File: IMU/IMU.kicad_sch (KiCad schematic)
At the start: 4 parts, among them IC1 ADXL326BCPZ-RL7, U1 DEV-16771, U2 IAM-20380, U3 MLX90393SLW-ABA-011-RE

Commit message: Finished Schematic!!!
Co-Authored-By: Ram Godbole <91348559+EnderScythe@users.noreply.github.com>
Co-Authored-By: Ayaan-Abrol <89829573+Ayaan-Abrol@users.noreply.github.com>
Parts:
- added C1, C2, C3: 3 nF, Capacitor_SMD:C_0603_1608Metric, symbol Device:C
- added C10, C6, C9: 0.1 uF, Capacitor_SMD:C_0603_1608Metric, symbol Device:C
- added C4: 0.01 uF, Capacitor_SMD:C_0603_1608Metric, symbol Device:C
- added C5: 0.47 uF, Capacitor_SMD:C_0603_1608Metric, symbol Device:C
- added C7: 2.2 uF, Capacitor_SMD:C_0603_1608Metric, symbol Device:C
- added C8: 10 nF, Capacitor_SMD:C_0603_1608Metric, symbol Device:C
- IC1: footprint ADXL326BCPZRL7 -> ADXL326BCPZ-RL7:ADXL326BCPZRL7
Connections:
- net 3P3V: now reaches U2.1 (VDDIO)
- net 3P3V: now also IC1.14 (VS_1), IC1.15 (VS_2), U1.3.3V_1 (3.3V), U1.3.3V_2 (3.3V__1), U1.3.3V_3 (3.3V__2), U2.16 (VDD), U3.15 (VDD), U3.8 (VDD_IO), C10.1, C4.1, C6.1, C7.1, C8.1, C9.1
- net GND: now reaches U2.10 (RESV)
- net GND: now also IC1.17 (EP), IC1.3 (COM_1), IC1.5 (COM_2), IC1.6 (COM_3), IC1.7 (COM_4), U2.11 (RESV), U2.12 (RESV), U2.13 (GND), U2.15 (RESV), U2.8 (FSYNC), U2.9 (RESV), U3.11 (A1), U3.12 (A0), U3.13 (VSS), U3.17 (GND), C1.2, C10.2, C2.2, C3.2, C4.2, C5.2, C6.2, C7.2, C8.2, C9.2
- net at U2.14 (REGOUT): now also C5.1
- net SCK_Gyro: now reaches U2.2 (SCL/SPC)
- net SCK_Gyro: now also U1.27 (A13)
- net MOSI_Gyro: now reaches U2.3 (SDA/SDI)
- net MOSI_Gyro: now also U1.26 (A12)
- net MISO_Gyro: now reaches U2.4 (SA0/SDO)
- net MISO_Gyro: now also U1.1 (TX1)
- net CS_Gyro: now reaches U2.5 (CS)
- net CS_Gyro: now also U1.0 (RX1)
- net INT_Gyro: now reaches U2.6 (INT)
- net INT_Gyro: now also U1.17 (A3)
- net CS_Mag: now reaches U1.10 (CS1)
- net CS_Mag: now also U3.2 (SENB/CS)
- net MOSI_Mag: now reaches U1.11 (MOSI)
- net MOSI_Mag: now also U3.5 (SDA/MOSI)
- net MISO_Mag: now reaches U1.12 (MISO)
- net MISO_Mag: now also U3.6 (MISO)
- net SCK_Mag: now reaches U1.13 (SCK)
- net SCK_Mag: now also U3.3 (SCL/SCLK)
- net X_Accel: now reaches U1.14 (A0)
- net X_Accel: now also IC1.12 (XOUT), C1.1
- net Y_Accel: now reaches U1.15 (A1)
- net Y_Accel: now also IC1.10 (YOUT), C2.1
- net Z_Accel: now reaches U1.16 (A2)
- net Z_Accel: now also IC1.8 (ZOUT), C3.1
- net INT_Mag: now reaches U1.18 (A4)
- net INT_Mag: now also U3.1 (INT)
- net TRIG_Mag: now reaches U1.19 (A5)
- net TRIG_Mag: now also U3.7 (INT/TRIG)
- no-connect marks 0 -> 7
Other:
- note added: "Accelerometer"
- note added: "Gyroscope"
- note added: "Magnetometer"
- moved on the sheet: U2

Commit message: Ground is important!
Co-Authored-By: Ram Godbole <91348559+EnderScythe@users.noreply.github.com>
Co-Authored-By: Ayaan-Abrol <89829573+Ayaan-Abrol@users.noreply.github.com>
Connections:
- net GND: now also U1.GND1 (GND), U1.GND2 (GND__1), U1.GND3 (GND__2), U1.GND4 (GND__3), U1.GND5 (GND__4), U1.USB_GND1 (USB_GND), U1.USB_GND2 (USB_GND__1)
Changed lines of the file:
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@@
+	)
+	(junction
+		(at 63.5 139.7)
+		(diameter 0)
+		(color 0 0 0 0)
 	)
 	(junction
@@
 	)
 	(junction
+		(at 63.5 134.62)
+		(diameter 0)
+		(color 0 0 0 0)
+	)
+	(junction
+		(at 63.5 142.24)
+		(diameter 0)
+		(color 0 0 0 0)
+	)
+	(junction
 		(at 219.71 90.17)
 		(diameter 0)
@@
 	)
 	(junction
+		(at 63.5 129.54)
+		(diameter 0)
+		(color 0 0 0 0)
+	)
+	(junction
 		(at 168.91 63.5)
 		(diameter 0)
@@
 	)
 	(junction
+		(at 63.5 137.16)
+		(diameter 0)
+		(color 0 0 0 0)
+	)
+	(junction
 		(at 224.79 45.72)
 		(diameter 0)
@@
 	(junction
 		(at 63.5 30.48)
+		(diameter 0)
+		(color 0 0 0 0)
+	)
+	(junction
+		(at 63.5 132.08)
 		(diameter 0)
 		(color 0 0 0 0)
@@
 	(wire
 		(pts
+			(xy 63.5 142.24) (xy 63.5 147.32)
+		)
+		(stroke
+			(width 0)
+			(type default)
+		)
+	)
+	(wire
+		(pts
 			(xy 248.92 73.66) (xy 245.11 73.66)
 		)
@@
 	(wire
 		(pts
+			(xy 63.5 137.16) (xy 63.5 139.7)
+		)
+		(stroke
+			(width 0)
+			(type default)
+		)
+	)
+	(wire
+		(pts
 			(xy 226.06 105.41) (xy 226.06 110.49)
 		)
@@
 	(wire
 		(pts
+			(xy 63.5 127) (xy 63.5 129.54)
+		)
+		(stroke
+			(width 0)
+			(type default)
+		)
+	)
+	(wire
+		(pts
 			(xy 168.91 63.5) (xy 168.91 66.04)
 		)
@@
 	(wire
 		(pts
+			(xy 63.5 132.08) (xy 63.5 134.62)
+		)
+		(stroke
+			(width 0)
+			(type default)
+		)
+	)
+	(wire
+		(pts
 			(xy 242.57 90.17) (xy 250.19 90.17)
 		)
@@
 	(wire
 		(pts
+			(xy 63.5 129.54) (xy 63.5 132.08)
+		)
+		(stroke
+			(width 0)
+			(type default)
+		)
+	)
+	(wire
+		(pts
 			(xy 168.91 66.04) (xy 168.91 72.39)
 		)
@@
 	(wire
 		(pts
+			(xy 63.5 134.62) (xy 63.5 137.16)
+		)
+		(stroke
+			(width 0)
+			(type default)
+		)
+	)
+	(wire
+		(pts
 			(xy 175.26 38.1) (xy 168.91 38.1)
+		)
+		(stroke
+			(width 0)
+			(type default)
+		)
+	)
+	(wire
+		(pts
+			(xy 63.5 139.7) (xy 63.5 142.24)
 		)
 		(stroke
@@
 		)
 	)
+	(label "GND"
+		(at 63.5 147.32 0)
+		(effects
+			(font
+				(size 1.27 1.27)
+			)
+			(justify left bottom)
+		)
+	)

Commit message: Some layout changes
Added filled zomes, linked 3d models, added board edge cuts and mounting holes (still need to add filled zone exclusions around the mounting holes to prevent shorts, though I will probably just reduced the filled zomes anyways. Also should probably change which analog pins get used for the Gyro before routing traces/vias.
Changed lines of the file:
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@@
 	(wire
 		(pts
-			(xy 63.5 142.24) (xy 63.5 147.32)
+			(xy 69.85 142.24) (xy 69.85 147.32)
 		)
 		(stroke
@@
 		(pts
 			(xy 241.3 69.85) (xy 237.49 69.85)
+		)
+		(stroke
+			(width 0)
+			(type default)
+		)
+	)
+	(wire
+		(pts
+			(xy 69.85 142.24) (xy 63.5 142.24)
 		)
 		(stroke
@@
 	)
 	(label "GND"
-		(at 63.5 147.32 0)
-		(effects
-			(font
+		(at 69.85 147.32 0)
+		(effects
+			(font

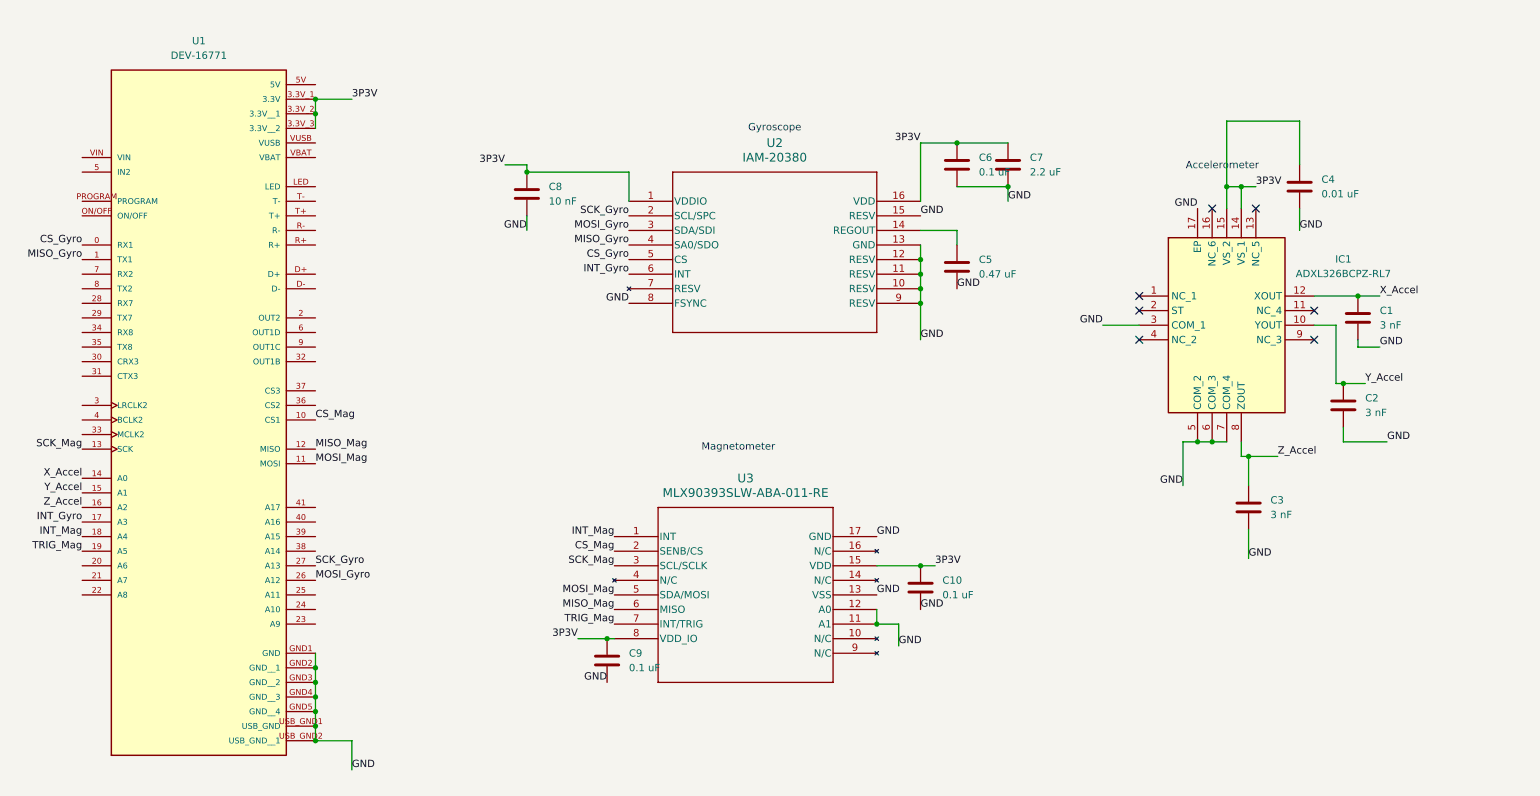
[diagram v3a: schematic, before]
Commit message: Update IMU.kicad_sch
Added a bunch of zero-ohm resistors to the digital pins in case we need to route overboard wires.
Also added some testpoints for 3.3 and 0 V
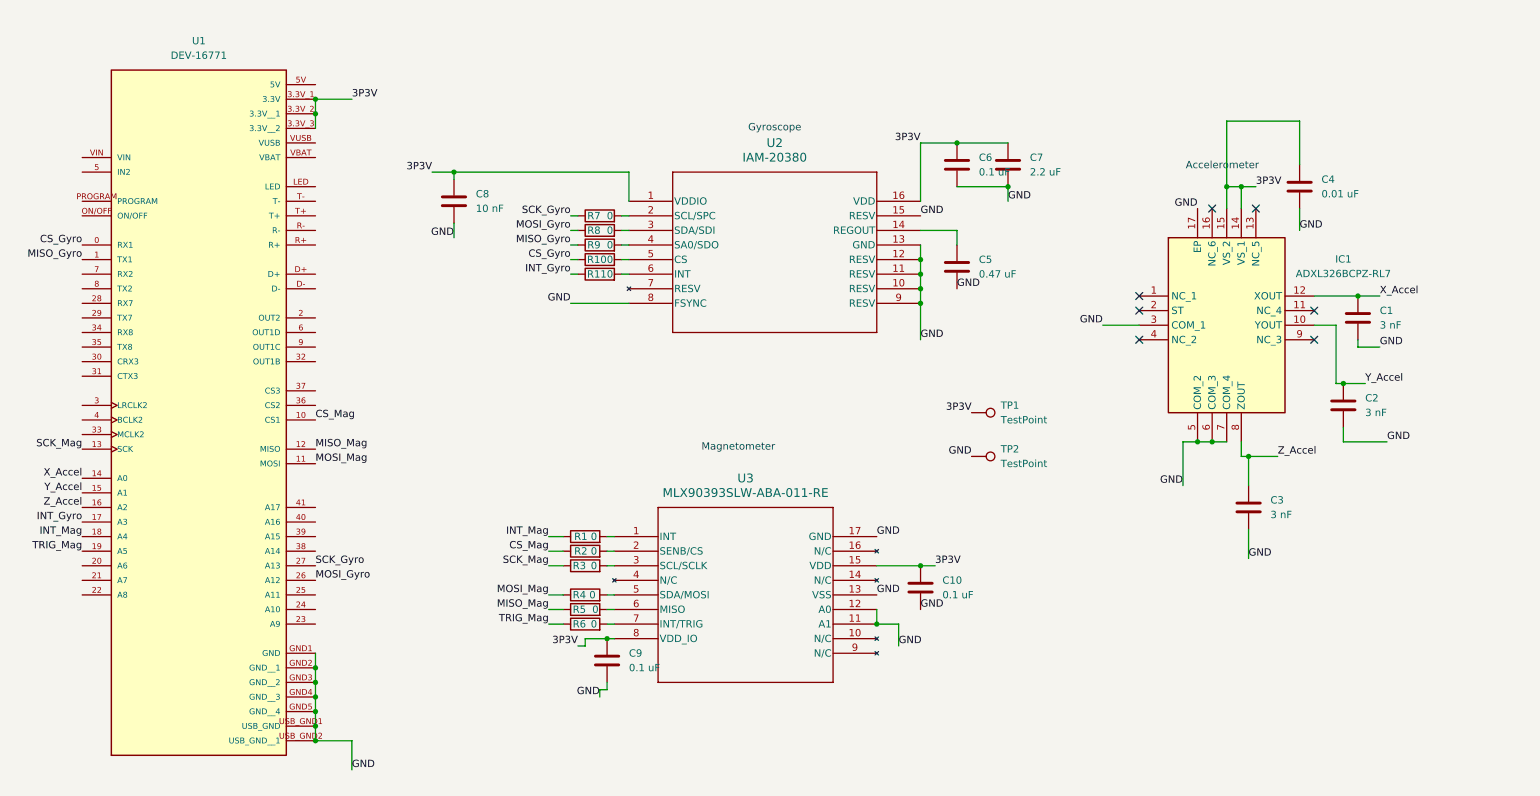
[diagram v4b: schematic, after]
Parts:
- added R1, R10, R11, R2, R3, R4, R5, R6, R7, R8, R9: 0, Resistor_SMD:R_0603_1608Metric, symbol Device:R
- added TP1, TP2: TestPoint, TestPoint:TestPoint_Pad_4.0x4.0mm, symbol Connector:TestPoint
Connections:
- net 3P3V: now also TP1.1
- net CS_Gyro: now also R10.1; no longer U2.5 (CS)
- net CS_Mag: now also R2.1; no longer U3.2 (SENB/CS)
- net GND: now also TP2.1
- net INT_Gyro: now also R11.1; no longer U2.6 (INT)
- net INT_Mag: now also R1.1; no longer U3.1 (INT)
- net MISO_Gyro: now also R9.1; no longer U2.4 (SA0/SDO)
- net MISO_Mag: now also R5.1; no longer U3.6 (MISO)
- net MOSI_Gyro: now also R8.1; no longer U2.3 (SDA/SDI)
- net MOSI_Mag: now also R4.1; no longer U3.5 (SDA/MOSI)
- net SCK_Gyro: now also R7.1; no longer U2.2 (SCL/SPC)
- net SCK_Mag: now also R3.1; no longer U3.3 (SCL/SCLK)
- net TRIG_Mag: now also R6.1; no longer U3.7 (INT/TRIG)
- new net: R5.2, U3.6 (MISO)
- new net: R6.2, U3.7 (INT/TRIG)
- new net: R4.2, U3.5 (SDA/MOSI)
- new net: R7.2, U2.2 (SCL/SPC)
- new net: R8.2, U2.3 (SDA/SDI)
- new net: R9.2, U2.4 (SA0/SDO)
- new net: R10.2, U2.5 (CS)
- new net: R11.2, U2.6 (INT)
- new net: R1.2, U3.1 (INT)
- new net: R2.2, U3.2 (SENB/CS)
- new net: R3.2, U3.3 (SCL/SCLK)
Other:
- moved on the sheet: C8

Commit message: Some minor Layout changes
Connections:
- no-connect marks 7 -> 45
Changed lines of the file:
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@@
+	)
+	(no_connect
+		(at 63.5 104.14)
+	)
+	(no_connect
+		(at 22.86 86.36)
+	)
+	(no_connect
+		(at 63.5 55.88)
 	)
 	(no_connect
 		(at 237.49 72.39)
+	)
+	(no_connect
+		(at 63.5 27.94)
+	)
+	(no_connect
+		(at 63.5 106.68)
 	)
 	(no_connect
@@
 	)
 	(no_connect
+		(at 63.5 81.28)
+	)
+	(no_connect
+		(at 22.86 71.12)
+	)
+	(no_connect
+		(at 63.5 68.58)
+	)
+	(no_connect
+		(at 63.5 76.2)
+	)
+	(no_connect
+		(at 63.5 45.72)
+	)
+	(no_connect
 		(at 207.01 72.39)
+	)
+	(no_connect
+		(at 63.5 48.26)
+	)
+	(no_connect
+		(at 22.86 48.26)
+	)
+	(no_connect
+		(at 63.5 60.96)
+	)
+	(no_connect
+		(at 63.5 53.34)
+	)
+	(no_connect
+		(at 22.86 78.74)
+	)
+	(no_connect
+		(at 63.5 109.22)
+	)
+	(no_connect
+		(at 22.86 40.64)
+	)
+	(no_connect
+		(at 22.86 66.04)
+	)
+	(no_connect
+		(at 63.5 38.1)
+	)
+	(no_connect
+		(at 22.86 116.84)
+	)
+	(no_connect
+		(at 22.86 43.18)
+	)
+	(no_connect
+		(at 22.86 68.58)
+	)
+	(no_connect
+		(at 63.5 101.6)
+	)
+	(no_connect
+		(at 63.5 71.12)
 	)
 	(no_connect
@@
 	)
 	(no_connect
+		(at 22.86 114.3)
+	)
+	(no_connect
+		(at 63.5 73.66)
+	)
+	(no_connect
+		(at 22.86 111.76)
+	)
+	(no_connect
+		(at 63.5 40.64)
+	)
+	(no_connect
+		(at 22.86 76.2)
+	)
+	(no_connect
+		(at 22.86 73.66)
+	)
+	(no_connect
 		(at 227.33 49.53)
+	)
+	(no_connect
+		(at 22.86 63.5)
+	)
+	(no_connect
+		(at 63.5 50.8)
+	)
+	(no_connect
+		(at 63.5 63.5)
+	)
+	(no_connect
+		(at 22.86 60.96)
+	)
+	(no_connect
+		(at 22.86 88.9)
+	)
+	(no_connect
+		(at 63.5 83.82)
 	)
 	(no_connect
 		(at 219.71 49.53)
 	)
+	(no_connect
+		(at 22.86 50.8)
+	)
+	(no_connect
+		(at 22.86 83.82)
+	)
 	(wire

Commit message: m
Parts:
- removed C1, C2, C3: 3 nF, Capacitor_SMD:C_0603_1608Metric, symbol Device:C
- removed C4: 0.01 uF, Capacitor_SMD:C_0603_1608Metric, symbol Device:C
- removed IC1: ADXL326BCPZ-RL7, ADXL326BCPZ-RL7:ADXL326BCPZRL7, symbol ADXL326BCPZ-RL7:ADXL326BCPZ-RL7
- removed R1, R10, R11, R2, R3, R4, R5, R6, R7, R8, R9: 0, Resistor_SMD:R_0603_1608Metric, symbol Device:R
- removed TP1, TP2: TestPoint, TestPoint:TestPoint_Pad_4.0x4.0mm, symbol Connector:TestPoint
- removed U1: DEV-16771, DEV-16771:DEV-16771, symbol DEV-16771:DEV-16771
- added U4: RASPBERRY_PI_PICO, Raspberry Pi:RASPBERRY_PI_PICO, symbol RASPBERRY_PI_PICO:RASPBERRY_PI_PICO
- added U5: ADXL380-1BCCZ-RL7, ADXL380:ADXL380, symbol ADXL380:ADXL380-1BCCZ-RL7
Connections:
- net 3P3V: now also U4.3V3, U5.10 (VS), U5.11 (VDDIO)
- net CS_Gyro: now also U2.5 (CS), U4.GP13
- net GND: now also U4.AGND, U4.GND, U4.GND2, U4.GND3, U4.GND4, U4.GND5, U4.GND6, U4.GND7, U5.9 (GND)
- net INT_Gyro: now also U2.6 (INT), U4.GP14
- net INT_Mag: now also U3.1 (INT), U4.GP8
- net MISO_Gyro: now also U2.4 (SA0/SDO), U4.GP12
- net MOSI_Gyro: now also U2.3 (SDA/SDI), U4.GP11
- net SCK_Gyro: now also U2.2 (SCL/SPC), U4.GP10
- net SCK_Mag: now also U3.3 (SCL/SCLK), U4.GP7
- net SDA_Mag: now reaches U3.5 (SDA/MOSI)
- net SDA_Mag: now also U4.GP6
- new net ACCEL_CS: U4.GP5, U5.5 (*CS/ASEL1)
- new net ACCEL_INT: U4.GP1, U5.6 (INT0)
- new net ACCEL_SCLK: U4.GP2, U5.2 (SCLK/SCL)
- new net ACCEL_SDI: U4.GP3, U5.3 (SDI/SDA)
- new net ACCEL_SDO: U4.GP4, U5.4 (SDO/ASEL0)
- no-connect marks 45 -> 8
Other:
- note added: "Acceleromter"
- note added: "Gyro SPI 1 Accel SPI 0 Mag I2C 0"
- note removed: "Accelerometer"

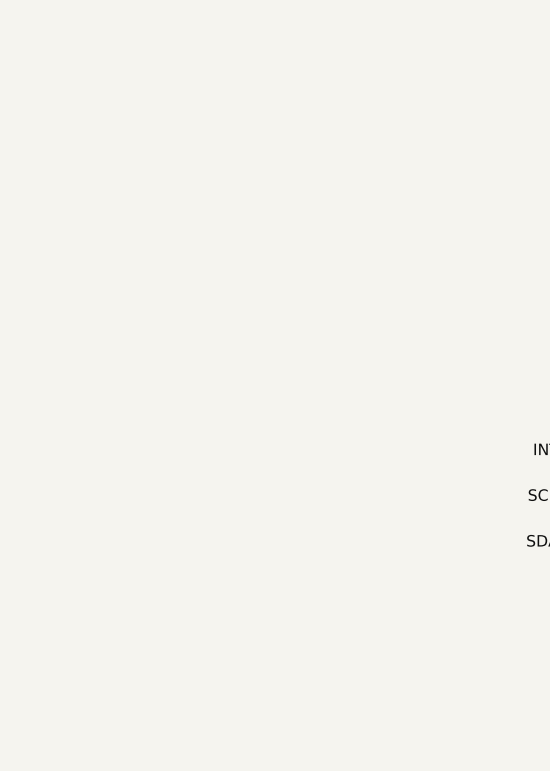
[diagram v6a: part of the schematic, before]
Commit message: fixed board size
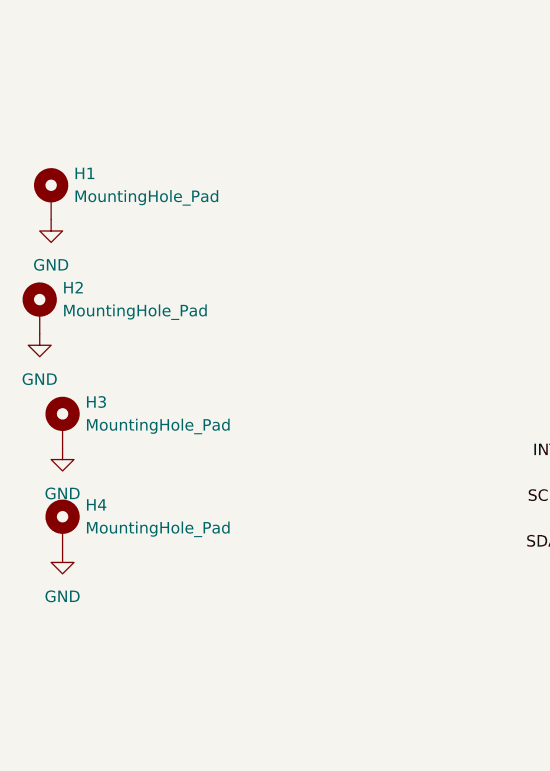
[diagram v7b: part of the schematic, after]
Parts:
- added H1, H2, H3, H4: MountingHole_Pad, MountingHole:MountingHole_3.2mm_M3_DIN965_Pad, symbol Mechanical:MountingHole_Pad
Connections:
- net GND: now also H1.1, H2.1, H3.1, H4.1

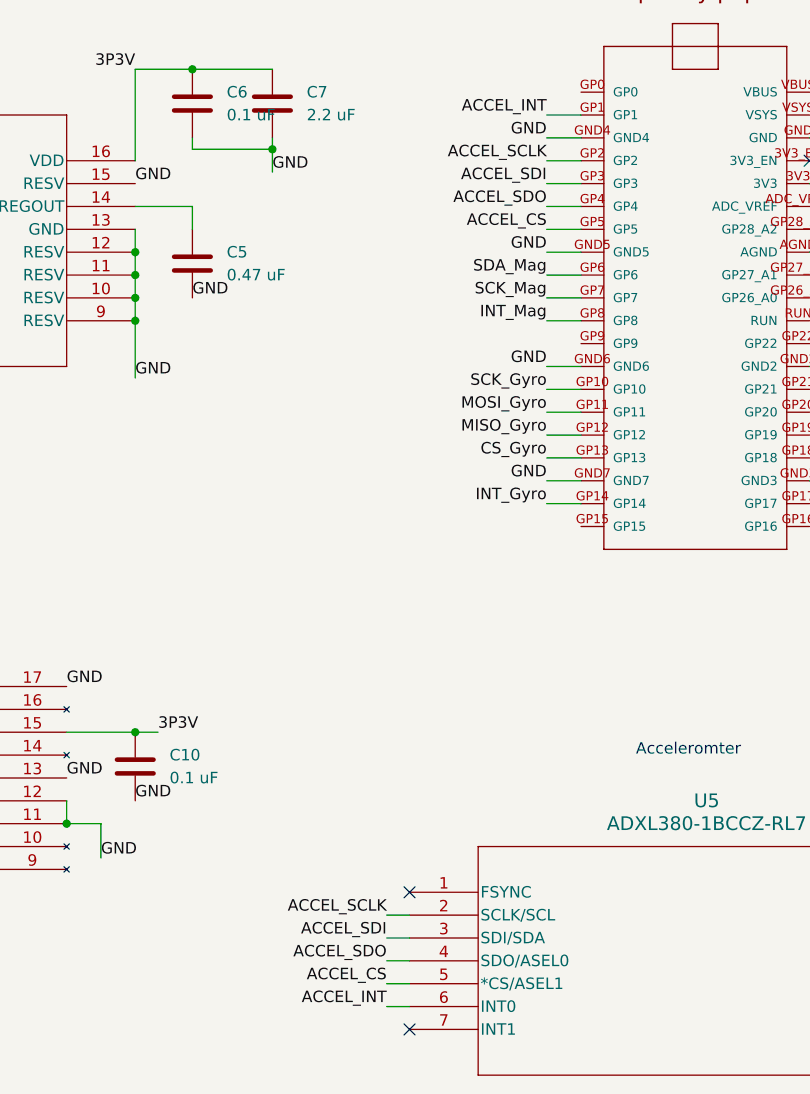
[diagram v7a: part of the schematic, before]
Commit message: Final Final Final Changes
Renamed accel SPI nets for clarity. Changed one of the internal planes to a power plane for 3P3V and removed 3P3V traces. Adjusted design constraints to eliminate DRC warnings/errors.
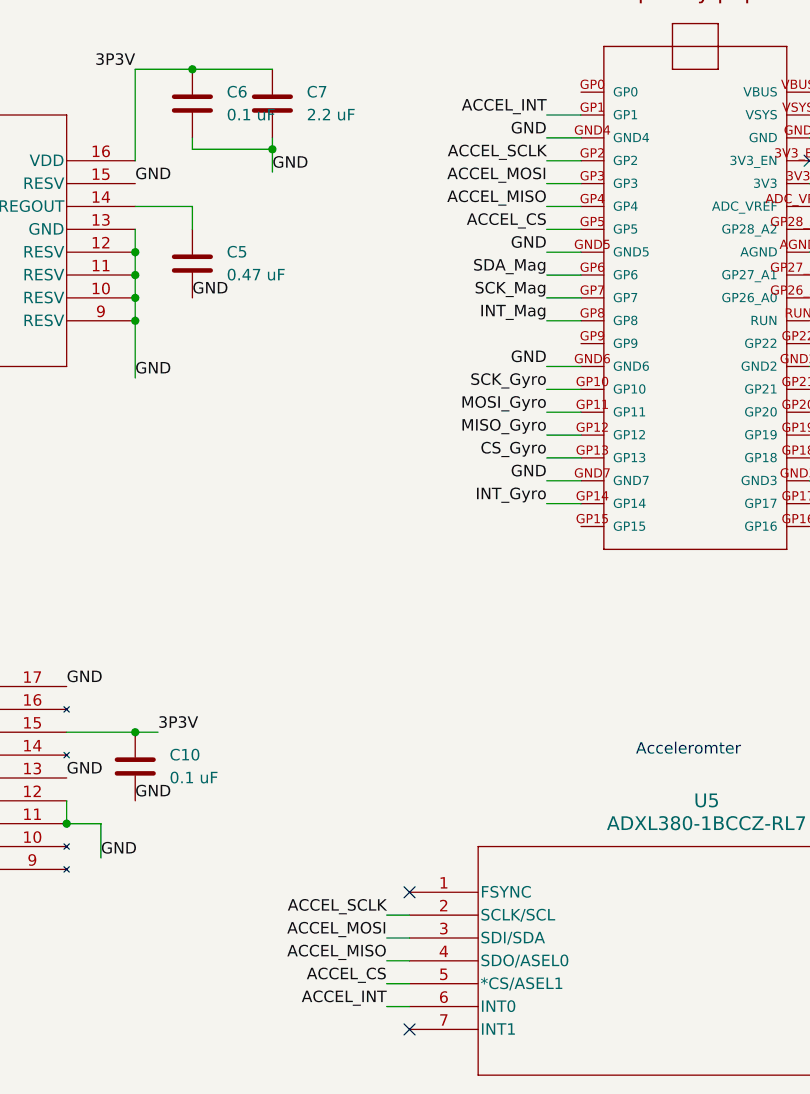
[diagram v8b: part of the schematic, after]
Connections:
- net ACCEL_SDI renamed ACCEL_MOSI
- net ACCEL_SDO renamed ACCEL_MISO
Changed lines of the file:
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@@
+		)
+	)
+	(label "ACCEL_MISO"
+		(at 214.63 53.34 180)
+		(effects
+			(font
+				(size 1.27 1.27)
+			)
+			(justify right bottom)
 		)
 	)
@@
 		)
 	)
-	(label "ACCEL_SDI"
+	(label "ACCEL_MOSI"
 		(at 196.85 134.62 180)
-		(effects
-			(font
-				(size 1.27 1.27)
-			)
-			(justify right bottom)
-		)
-	)
-	(label "ACCEL_SDI"
-		(at 214.63 50.8 180)
 		(effects
 			(font
@@
 		)
 	)
+	(label "ACCEL_MOSI"
+		(at 214.63 50.8 180)
+		(effects
+			(font
+				(size 1.27 1.27)
+			)
+			(justify right bottom)
+		)
+	)
 	(label "GND"
 		(at 248.92 45.72 0)
@@
 		)
 	)
-	(label "ACCEL_SDO"
-		(at 214.63 53.34 180)
-		(effects
-			(font
-				(size 1.27 1.27)
-			)
-			(justify right bottom)
-		)
-	)
-	(label "ACCEL_SDO"
+	(label "ACCEL_MISO"
 		(at 196.85 137.16 180)
 		(effects
